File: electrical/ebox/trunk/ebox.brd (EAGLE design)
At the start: 100 x 80 mm, 157 parts, among them IC1 MAX3221CUE, IC10 SN74LVC1G125, IC11 MAX3221CUE, IC12 INA170, IC13 SN74LVC1G125, IC14 SN74LVC1G125, IC15 MAX3221CUE, IC16 MCP170333MB, IC17 SN74LVC1G125, IC18 SN74LVC1G125, IC19 74ALS04D, IC2 LT3652, IC3 XMEGA128A1, IC4 LT1161, IC5 SN74LVC1G125, IC6 SN74LVC1G125, IC7 MAX3221CUE, IC8 INA170, IC9 SN74LVC1G125, Q1 FDD4141TO252, U1 BLUETOOTH-RN42, U2 D2523T_, X1 BULLET, X10 DEANS-MALE, X11 DEANS-MALE, X12 7381-2PG-300, X13 B4B-ZR, X14 BULLET, X15 DEANS-FEMALE, X16 DEANS-FEMALE, X17 22-23-2021, X18 7381-3PG-300, X19 7381-3PG-300, X2 BULLET, X20 BULLET, X21 BULLET, X22 BULLET, X23 BULLET, X24 B4B-ZR, X3 17984-7PG-300, X4 BULLET, X5 17984-7PG-300, X6 17984-7PG-300, X7 17984-7PG-300, X8 22-23-2031, X9 22-23-2031

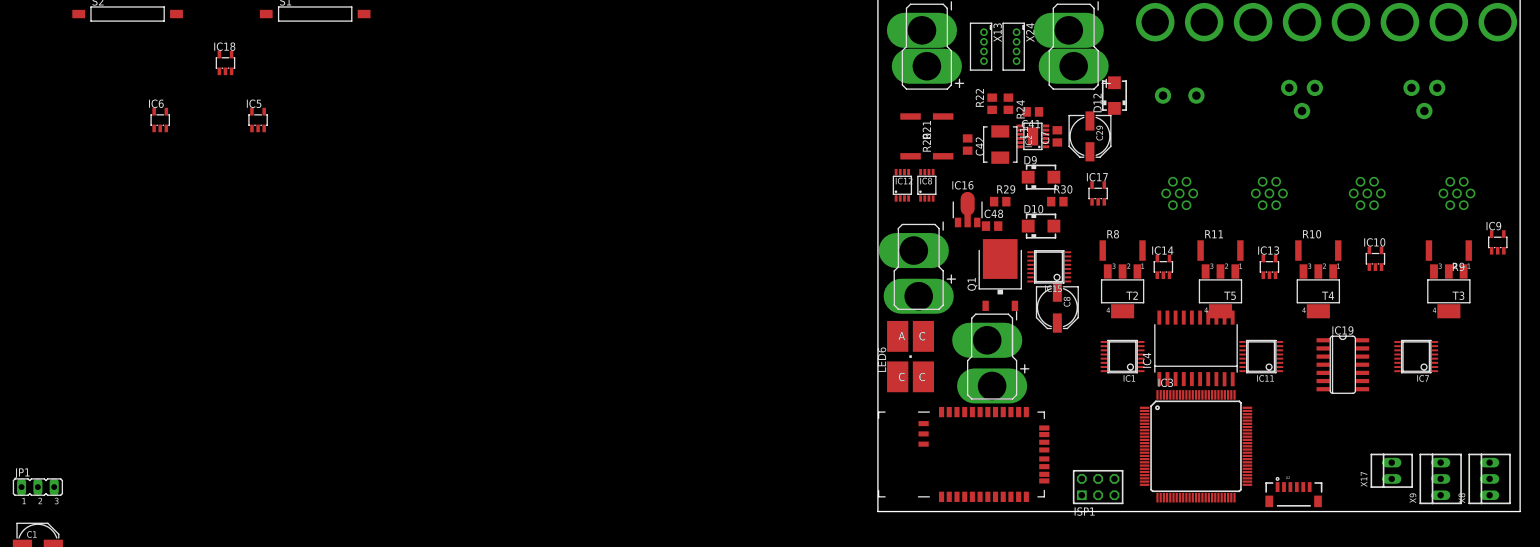
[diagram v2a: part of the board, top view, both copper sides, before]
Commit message: Added USB connector, swapped FETs for smaller form factor.
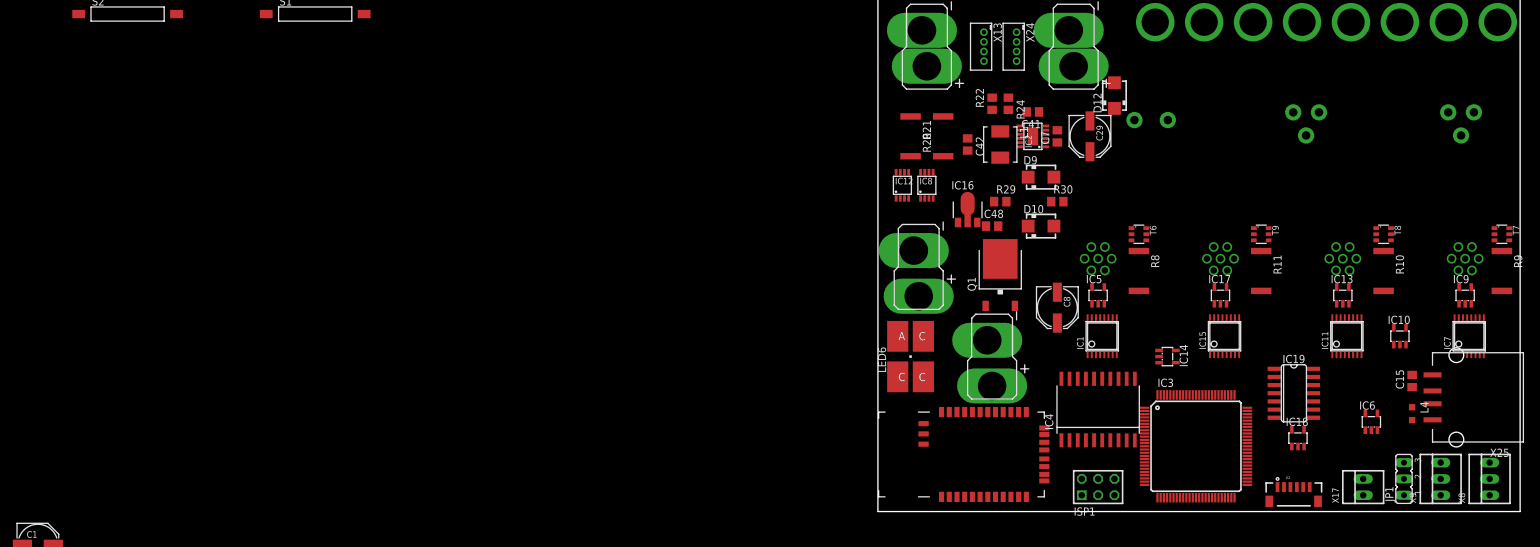
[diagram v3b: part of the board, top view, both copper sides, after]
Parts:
- removed T2, T3, T4, T5: (no value), zetex:SOT223
- added C15: 10uF, rcl:C0805
- added L4: 10uH, rcl:L2012C
- added T6, T7, T8, T9: (no value), zetex:SOT23-6
- added X25: USB_A, crw:1001-002-01100
- moved JP1 212.7 mm to (81.9, 5.08), turned to 90 degrees
- moved IC6 194.4 mm to (76.8, 14.0)
- moved IC18 176.9 mm to (65.4, 11.4)
- moved IC5 133.6 mm to (34.3, 33.7)
- moved IC15 29.4 mm to (54.0, 27.3), turned to 0 degrees
- moved IC17 24.8 mm to (53.3, 33.7)
- moved IC4 18.0 mm to (34.3, 15.9)
- moved X3 16.3 mm to (34.3, 39.4)
- moved IC14 14.0 mm to (45.1, 24.1), turned to 270 degrees
- moved IC11 13.7 mm to (73.0, 27.3), turned to 0 degrees
- moved X7 12.7 mm to (53.3, 39.4)
- moved IC10 12.7 mm to (81.3, 27.3)
- moved IC13 12.3 mm to (72.4, 33.7)
- moved X6 10.9 mm to (72.4, 39.4)
- moved R10 10.6 mm to (78.7, 37.5), turned to 270 degrees
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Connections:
- new net N$40: C15.1, L4.1, X25.1
- new net N$45: X25.2, X25.3
- net +5V: now also L4.2
- net GND: now also C15.2, X25.4
- net N$12: now also T6.1, T6.2, T6.5, T6.6; no longer T2.2
- net N$14: now also T7.1, T7.2, T7.5, T7.6; no longer T3.2
- net N$15: now also T8.1, T8.2, T8.5, T8.6; no longer T4.2
- net N$16: now also T9.1, T9.2, T9.5, T9.6; no longer T5.2
- net N$17: now also T6.4; no longer T2.1
- net N$18: now also T7.4; no longer T3.1
- net N$19: now also T8.4; no longer T4.1
- net N$20: now also T9.4; no longer T5.1
- net S1_12V: now also T6.3; no longer T2.3
- net S2_12V: now also T7.3; no longer T3.3
- net S3_12V: now also T8.3; no longer T4.3
- net S4_12V: now also T9.3; no longer T5.3

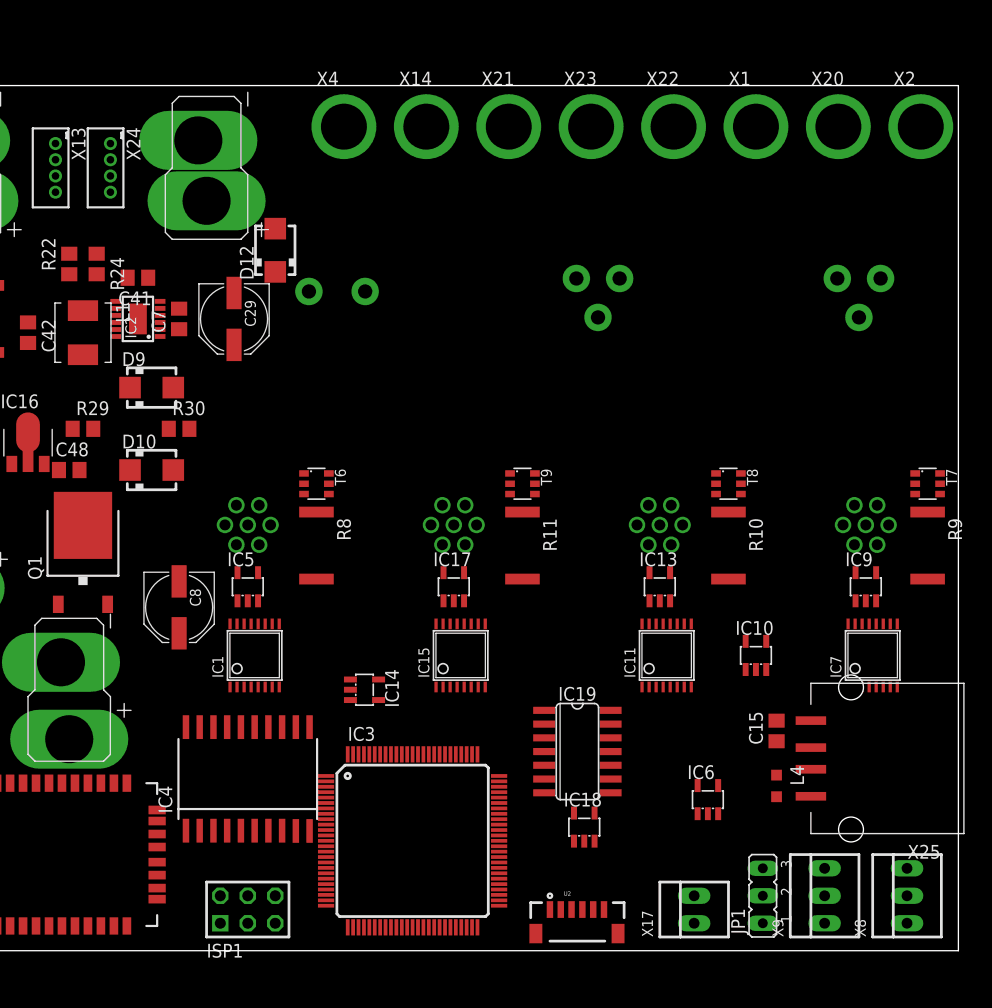
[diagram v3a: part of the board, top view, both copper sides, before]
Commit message: Generally figured out better layout for connectors, renamed some stuff for clarity.
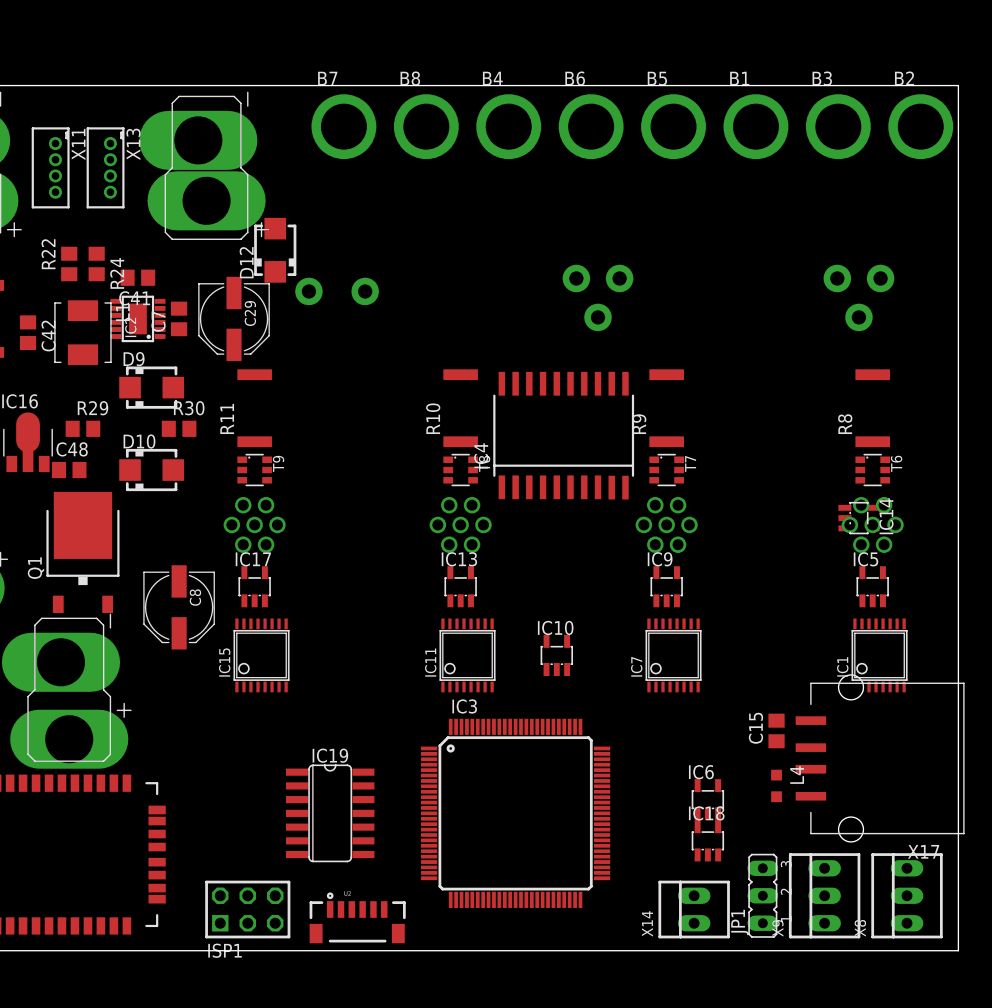
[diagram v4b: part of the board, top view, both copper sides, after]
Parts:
- removed X18, X19: 7381-3PG-300, crw:7381-3PG-300
- removed X24: B4B-ZR, con-jst:B4B-ZR
- removed X25: USB_A, crw:1001-002-01100
- added B1, B2, B7, B8: BULLET, crw:BULLET
- X1, X2: value BULLET -> 7381-3PG-300; device crw:BULLET -> crw:7381-3PG-300
- X11: value DEANS-MALE -> B4B-ZR; device crw:DEANS_MALE -> con-jst:B4B-ZR
- X12: value 7381-2PG-300 -> DEANS-MALE; device crw:7381-2PG-300 -> crw:DEANS_MALE
- X14: value BULLET -> 22-23-2021; device crw:BULLET -> con-molex:22-23-2021
- X17: value 22-23-2021 -> USB_A; device con-molex:22-23-2021 -> crw:1001-002-01100
- X3: value 17984-7PG-300 -> 7381-2PG-300; device crw:17984-7PG-300 -> crw:7381-2PG-300
- X4: value BULLET -> 17984-7PG-300; device crw:BULLET -> crw:17984-7PG-300
- moved X14 76.5 mm to (75.6, 3.81), turned to 90 degrees
- moved X4 61.2 mm to (92.1, 39.4), flipped to the bottom
- moved IC5 57.8 mm to (92.1, 33.7)
- moved IC1 57.8 mm to (92.7, 27.3)
- moved R8 53.0 mm to (92.1, 50.2), turned to 90 degrees
- moved T6 51.5 mm to (92.1, 44.5)
- moved IC14 48.4 mm to (90.8, 40.0)
- moved IC4 43.1 mm to (63.5, 47.6)
- moved X2 33.5 mm to (66.7, 61.0), flipped to the bottom
- moved R11 27.8 mm to (34.9, 50.2), turned to 90 degrees
- moved R10 27.8 mm to (54.0, 50.2), turned to 90 degrees
- moved R9 27.3 mm to (73.0, 50.2), turned to 90 degrees
- moved T9 24.8 mm to (34.9, 44.5)
- moved T8 24.8 mm to (54.0, 44.5)
- moved T7 24.2 mm to (73.0, 44.5)
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- renumbered X20 to B3, X21 to B4, X22 to B5, X23 to B6
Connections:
- net BATT+: now also X11.4, X12.POS; no longer X11.POS, X24.4
- net BATT-: now also X11.1, X12.NEG; no longer X11.NEG, X24.1
- net BATT1: now also X11.2; no longer X24.2
- net BATT2: now also X11.3; no longer X24.3
- net BATT_TEMP: now also X14.1; no longer X17.1
- net CHARGE: now also B7.P$1, X3.1; no longer X12.1, X4.P$1
- net GND: now also B8.P$1, X14.2, X17.4, X3.2, X4.7; no longer X12.2, X14.P$1, X17.2, X25.4, X3.7
- net MOT1_A: now also B1.P$1, X1.1; no longer X1.P$1, X18.1
- net MOT1_B: now also B2.P$1, X1.2; no longer X18.2, X2.P$1
- net MOT1_C: now also X1.3; no longer X18.3
- net MOT2_A: now also X2.1; no longer X19.1
- net MOT2_B: now also X2.2; no longer X19.2
- net MOT2_C: now also X2.3; no longer X19.3
- net N$40: now also X17.1; no longer X25.1
- net N$45: now also X17.2, X17.3; no longer X25.2, X25.3
- net S1_12V: now also X4.1; no longer X3.1
- net S1_5V: now also X4.4; no longer X3.4
- net S1_GPIO_A: now also X4.5; no longer X3.5
- net S1_GPIO_B: now also X4.6; no longer X3.6
- net S1_RX: now also X4.2; no longer X3.2
- net S1_TX: now also X4.3; no longer X3.3

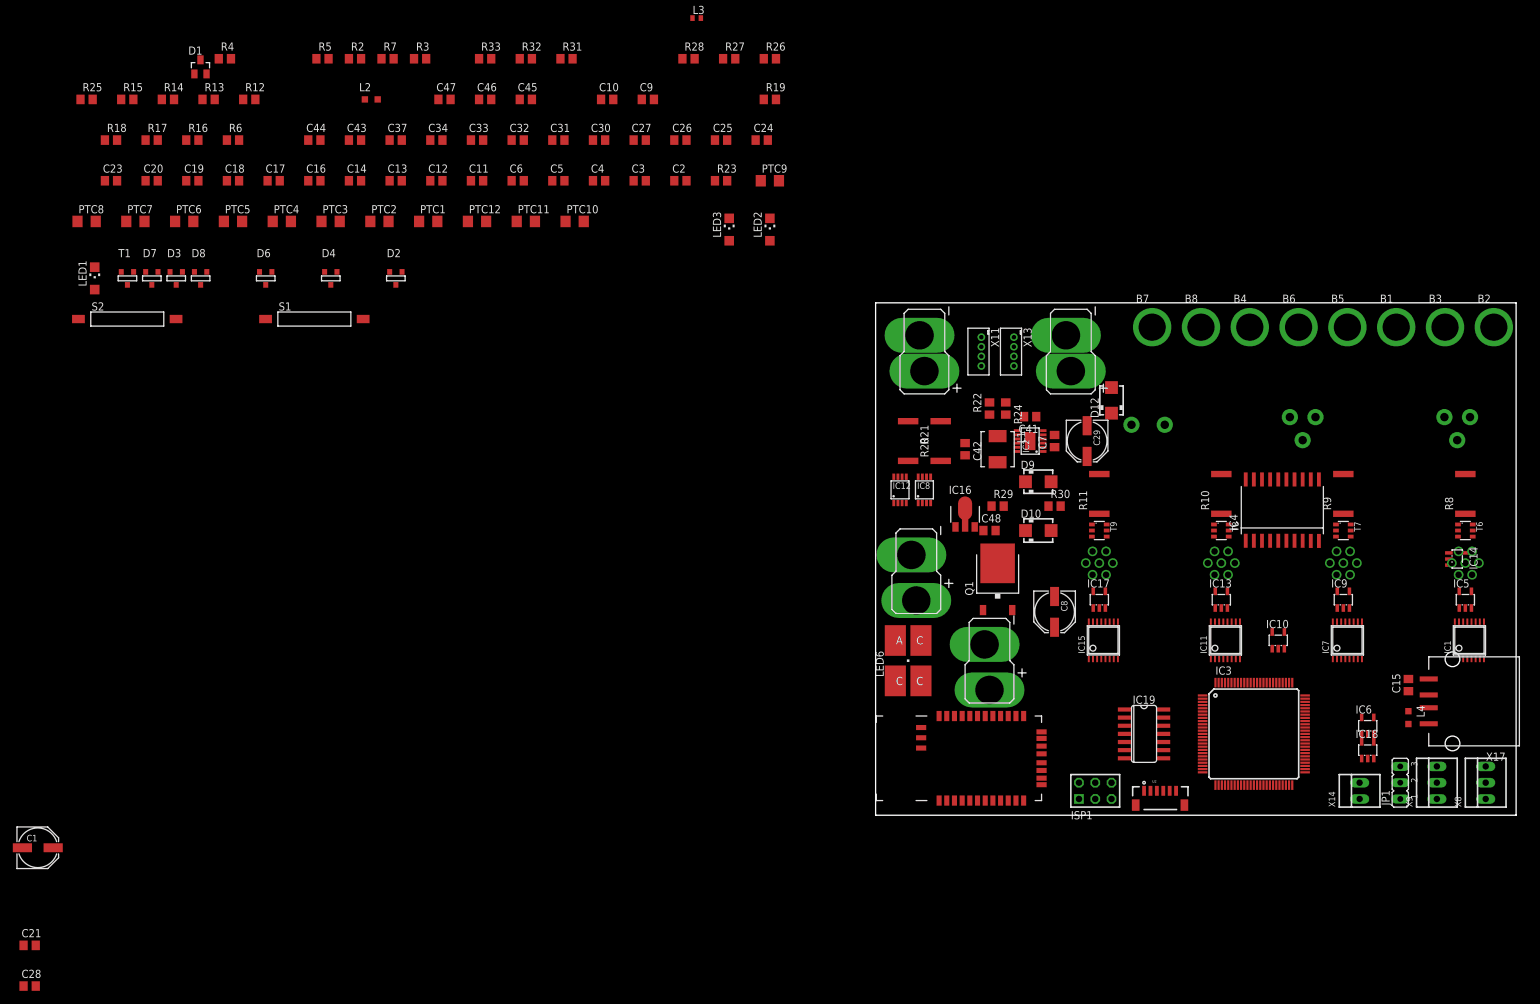
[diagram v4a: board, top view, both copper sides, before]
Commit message: Most of power layout is done too.
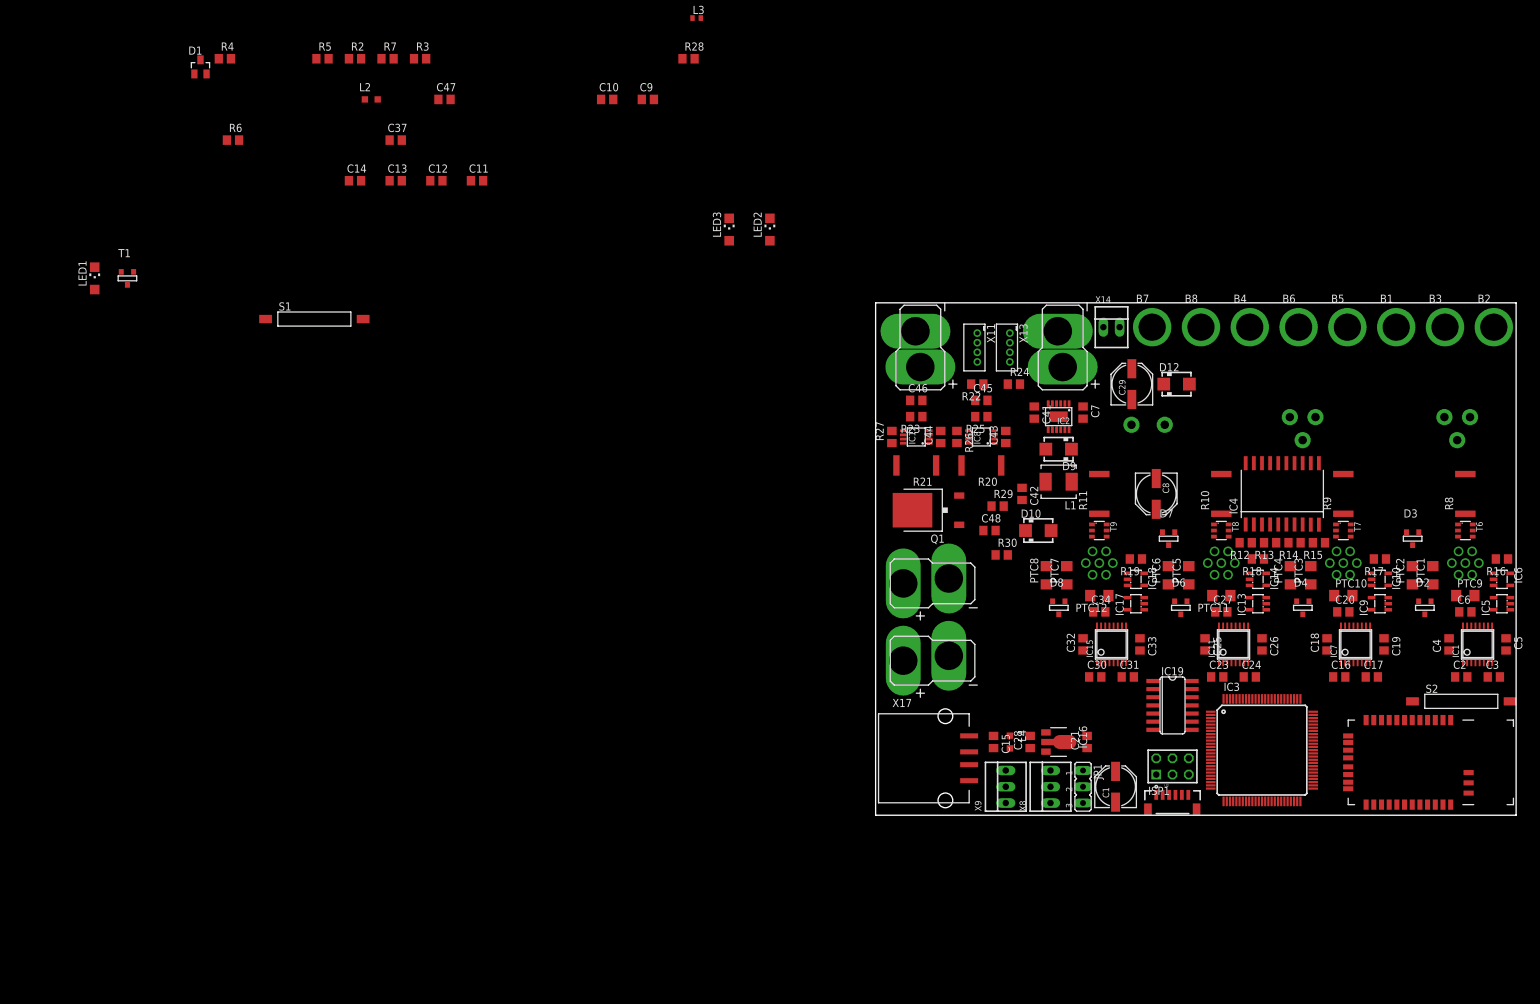
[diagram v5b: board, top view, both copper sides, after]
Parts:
- removed LED6: (no value), led:P-LCC-4
- removed R31, R32, R33: 330, rcl:R0805
- moved S2 216.7 mm to (91.4, 17.8)
- moved R16 214.7 mm to (97.8, 40.0), turned to 180 degrees
- moved R17 202.6 mm to (78.7, 40.0), turned to 180 degrees
- moved C19 199.6 mm to (79.4, 26.7), turned to 270 degrees
- moved R15 198.5 mm to (69.2, 42.5), turned to 180 degrees
- moved C20 197.9 mm to (73.0, 31.8)
- moved D3 197.3 mm to (83.8, 43.2)
- moved R18 190.6 mm to (59.7, 40.0), turned to 180 degrees
- moved C23 189.3 mm to (53.3, 21.6)
- moved R14 189.0 mm to (65.4, 42.5), turned to 180 degrees
- moved C17 188.1 mm to (77.5, 21.6)
- moved C18 185.5 mm to (70.5, 26.7), turned to 90 degrees
- moved R13 179.6 mm to (61.6, 42.5), turned to 180 degrees
- moved C16 177.8 mm to (72.4, 21.6)
- moved PTC2 170.5 mm to (83.8, 37.5), turned to 90 degrees
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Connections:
- removed net LED_BLU: IC3.19, R32.1
- removed net LED_GRN: IC3.16, R33.1
- removed net LED_RED: IC3.15, R31.1
- removed net N$51: LED6.C@3, R32.2
- removed net N$52: LED6.C@1, R31.2
- removed net N$53: LED6.C@4, R33.2
- net +3V3: no longer LED6.A

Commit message: Placed all components on board.
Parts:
- added R1, R31: 1k, rcl:R0805
- moved R7 213.7 mm to (106.7, 7.62), turned to 180 degrees
- moved C14 198.6 mm to (104.1, 27.9), turned to 180 degrees
- moved R2 190.2 mm to (78.7, 15.2)
- moved LED1 184.7 mm to (53.3, 25.4)
- moved L2 171.7 mm to (71.1, 27.9)
- moved C12 168.3 mm to (78.7, 17.8)
- moved C11 161.5 mm to (78.7, 20.3)
- moved C47 159.4 mm to (53.3, 7.62)
- moved D1 155.4 mm to (25.4, 33.0), turned to 270 degrees
- moved LED2 153.2 mm to (111.8, 7.62), turned to 270 degrees
- moved R3 153.2 mm to (50.8, 25.4), turned to 90 degrees
- moved C10 149.9 mm to (78.7, 22.9)
- moved R4 148.8 mm to (25.4, 40.6), turned to 180 degrees
- moved T1 146.6 mm to (25.4, 48.3), turned to 270 degrees
- moved C9 143.3 mm to (78.7, 25.4)
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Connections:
- new net N$46: R1.1, X13.3
- new net N$51: R31.1, X13.2
- net BATT1: now also R31.2; no longer X13.2
- net BATT2: now also R1.2; no longer X13.3
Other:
- board size 100 x 80 mm -> 127 x 101.6 mm
